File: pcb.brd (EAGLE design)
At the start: 88.9 x 70.1 mm, 104 parts, among them CN1 NC182M25, P1 39-30-02?, U1 TLV2242_D_8, U2 LT1117-S, U2.1 TCA6416A_PW_24, U3 SN74LVC1G17DBV, U4 SN74LVC1G17DBV, U6.1 DCH010505S_EDJ_4, U6.2 ISO7221A_D_8, U6.3 TS5A3357_DCU_8, U6.4 TS5A3357_DCU_8, U8.1 DCH010505S_EDJ_4, U8.2 MAX232E_D_16, U8.3 ISO7221A_D_8, U9.1 DCH010505S_EDJ_4, U9.2 ISO7220D, Y1 16MHZ

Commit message: Routing complete
All placement complete and signals routed. Awaiting copper planes,
renaming components, name placement and silkscreen.
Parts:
- removed R9.1: 47K, adafruit:M1206
- removed R9.3: 1.2K, adafruit:M1206
- added R14: 47K, rc-master-smd:R0603
- added R15: 1.2K, rc-master-smd:R0603
- moved H9.2 443.8 mm to (21.0, 68.6), turned to 180 degrees
- moved C40 440.4 mm to (13.2, 63.8)
- moved U4 437.1 mm to (13.2, 66.3), turned to 90 degrees
- moved C39 423.6 mm to (13.2, 58.7)
- moved U3 420.1 mm to (13.2, 61.2), turned to 90 degrees
- moved CN1 397.9 mm to (4.83, 45.5), turned to 90 degrees
- moved R21 369.5 mm to (71.1, 30.2), turned to 270 degrees
- moved R20 363.4 mm to (61.7, 30.2), turned to 270 degrees
- moved R19 359.4 mm to (63.5, 30.2), turned to 270 degrees
- moved R18 356.3 mm to (69.1, 30.2), turned to 270 degrees
- moved R22 345.3 mm to (24.1, 8.38), turned to 90 degrees
- moved P1 336.5 mm to (10.9, 12.2), turned to 270 degrees
- moved D4 312.4 mm to (66.3, 31.2), turned to 180 degrees
- moved D3 294.6 mm to (71.4, 18.0)
- moved D5 294.4 mm to (55.9, 8.64), turned to 90 degrees
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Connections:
- removed net 5VIO-4: D4.4, R20.1
- new net N$17: H6.1.1, R21.2
- new net N$31: H6.1.3, R18.2
- new net N$34: H6.1.5, R19.2
- new net N$35: H6.1.7, R20.2
- net 3VIO-0H: now also D3.4; no longer D3.1
- net 3VIO-2H: now also D3.1; no longer D3.4
- net 3VIO-3H: now also D2.4; no longer D2.6
- net 3VIO-4H: now also D2.3; no longer D2.1
- net 3VIO-5H: now also D2.1; no longer D2.3
- net 3VIO-6H: now also D2.6; no longer D2.4
- net 5VIO-0: now also D4.1, R21.1; no longer H6.1.7, R20.2
- net 5VIO-1: now also R18.1; no longer H6.1.5, R19.2, R21.1
- net 5VIO-2: now also D4.4, R19.1; no longer D4.1, H6.1.3, R18.1, R18.2
- net 5VIO-3: now also R20.1; no longer H6.1.1, R19.1, R21.2
- net LASER_CURRENT_3V: now also MCU.8; no longer MCU.5
- net LASER_ILK: now also R14.2; no longer R9.1.2
- net LASER_ILK_HIGH: now also R14.1; no longer R9.1.1
- net LASER_TEMPERATURE_3V: now also MCU.5; no longer MCU.8
- net N$14: now also R15.2; no longer R9.3.1
- net N$19: now also R15.1; no longer R9.3.2
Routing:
- net GND: track 123.1 -> 595.2 mm, vias 3 -> 12
- net +5V: track 86.1 -> 337.8 mm, vias 3 -> 8
- net +3V3: track 5.92 -> 249.9 mm, vias 0 -> 12
- net SGND: track 4.78 -> 45.9 mm, vias 0 -> 1
- net RS232_RX: track 37.0 -> 10.9 mm
- net TTL_GND_ISO: track 22.2 -> 43.1 mm
- net RS232_TX: track 34.2 -> 13.3 mm
- net EXT_TTL: track 10.7 -> 26.2 mm
- net 5VIO-0: track 39.0 -> 54.0 mm, vias 0 -> 4
- net N$11: track 0.00 -> 14.6 mm
- net 5VIO-2: track 31.2 -> 45.5 mm, vias 0 -> 4
- net LASER_TTL: track 63.9 -> 78.2 mm, vias 0 -> 2
- net 5VIO-3: track 26.7 -> 39.9 mm, vias 0 -> 2
- net N$14: track 0.00 -> 13.0 mm
- net N$8: track 0.00 -> 12.7 mm, vias 0 -> 1
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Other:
- board size 88.9 x 70.1 mm -> 88.9 x 81.3 mm

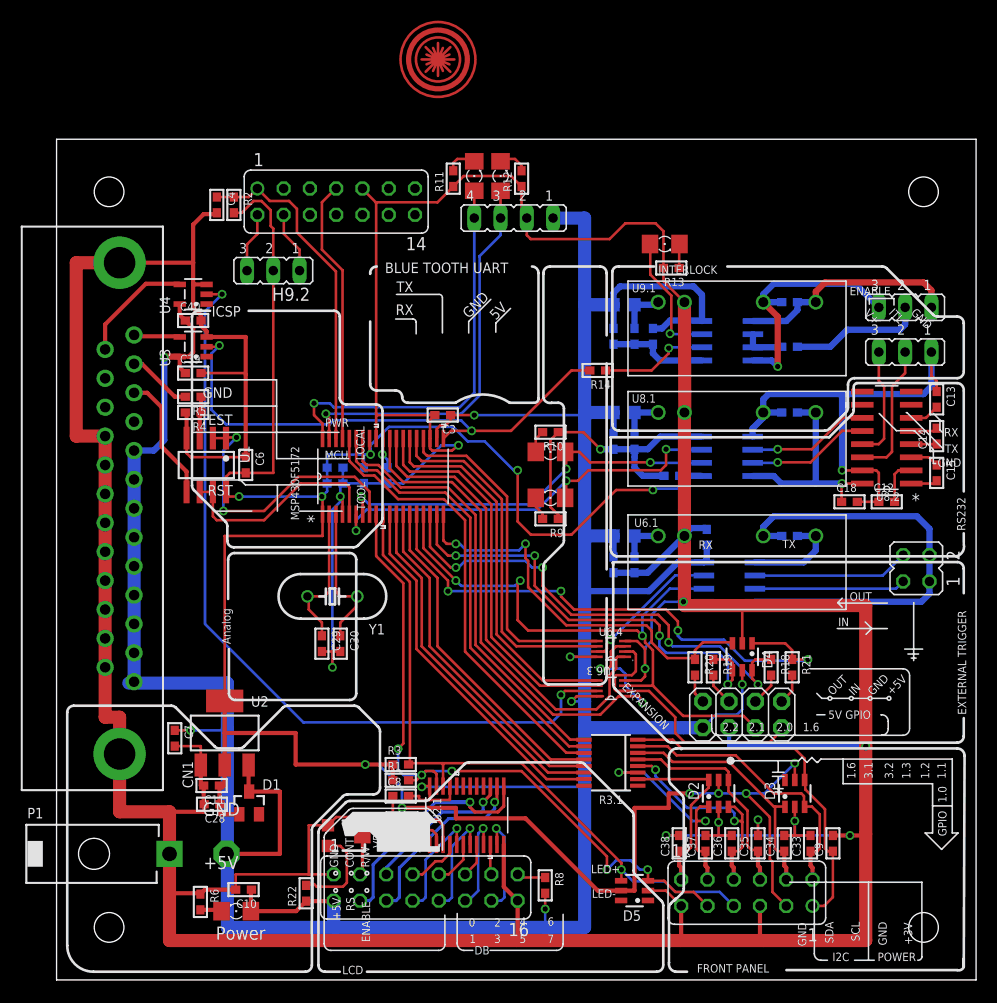
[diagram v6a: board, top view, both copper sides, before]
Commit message: Copper Pours & Component Silk Complete
Poured Copper planes and adjusted component designators for proper
silkscreen printing. Renumbered components.
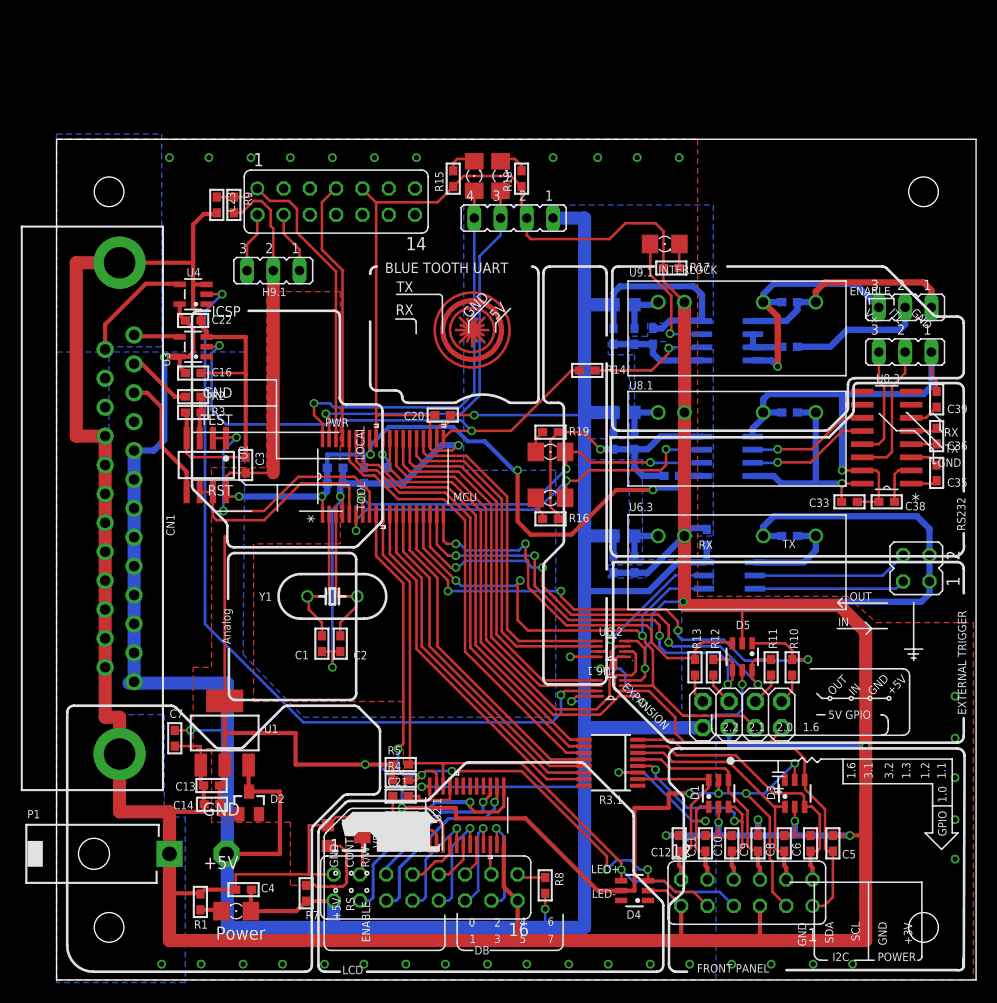
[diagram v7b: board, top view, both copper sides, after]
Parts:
- removed R21, R22: 330, rc-master-smd:R0603
- added R16, R17: 330, rc-master-smd:R0603
- C1: value .1uF -> 22pF
- C10, C5: value 10uF -> .1uF
- C14: value 1uF -> 10uF
- C15: value 1uF -> .1uF
- C17, C26: value 10uF -> 4.7uF
- C19: value 2.2uF -> .47uF
- C2: value .47uF -> 22pF
- C20, C22, C31: value 4.7uF -> .1uF
- C21: value 2.2uF -> .1uF
- C23: value .1uF -> 2.2nF
- C24: value 2.2uF -> 4.7uF
- C27: value .1uF -> 2.2uF
- C28: value 10uF -> 2.2uF
- C29: value 22pF -> 2.2uF
- C30: value 22pF -> .1uF
- C34, C37, C40: value .1uF -> 10uF
- C35, C36: value .1uF -> 1uF
- C4: value 2.2nF -> 10uF
- D1: value BAS70 -> SRV05-4; device diode:SOT23 -> diode:SOT23-6L
- D2: value SRV05-4 -> BAS70; device diode:SOT23-6L -> diode:SOT23
- H8.1: device jumper:JP2 -> jumper:JP4
- H8.2: device jumper:JP4 -> jumper:JP2
- R1, R15: value 1.2K -> 330
- R2: value 47K -> 400K
- R20: value 330 -> 1.2K
- R3: value 1.2K -> 600K
- R4: value 600K -> 1.2K
- R5: value 400K -> 1.2K
- R6: value 330 -> 10K
- R7: value 10K -> 330
- R9: value 330 -> 47K
- U1: value TLV2242_D_8 -> LT1117-S; device op-amp:SO08 -> v-reg:SOT223
- U2: value LT1117-S -> TLV2242_D_8; device v-reg:SOT223 -> op-amp:SO08
- U6.1: value DCH010505S_EDJ_4 -> TS5A3357_DCU_8; device TI:EDJ4 -> TI:DCU8
- U6.2: value ISO7221A_D_8 -> TS5A3357_DCU_8; device TI:D8 -> TI:DCU8
- U6.3: value TS5A3357_DCU_8 -> DCH010505S_EDJ_4; device TI:DCU8 -> TI:EDJ4
- U6.4: value TS5A3357_DCU_8 -> ISO7221A_D_8; device TI:DCU8 -> TI:D8
- U8.2: value MAX232E_D_16 -> ISO7221A_D_8; device TI:D16 -> TI:D8
- U8.3: value ISO7221A_D_8 -> MAX232E_D_16; device TI:D8 -> TI:D16
- moved C13 79.4 mm to (15.0, 18.8), turned to 180 degrees
- moved C14 78.6 mm to (15.0, 17.0), turned to 180 degrees
- moved C39 71.9 mm to (85.1, 56.1), turned to 270 degrees
- moved C4 66.2 mm to (18.1, 8.73), turned to 180 degrees
- moved C6 65.7 mm to (72.9, 13.2), turned to 90 degrees
- moved C15 62.8 mm to (32.5, 14.7)
- moved H9.1 61.2 mm to (21.0, 68.6)
- moved H9.2 61.2 mm to (82.0, 65.0)
- moved C40 58.3 mm to (70.9, 54.9), flipped to the bottom
- moved R11 56.4 mm to (69.1, 30.2), turned to 270 degrees
- moved R18 53.0 mm to (45.0, 77.5), turned to 90 degrees
- moved C34 52.3 mm to (70.9, 65.5), flipped to the bottom, turned to 180 degrees
- moved R12 50.8 mm to (63.5, 30.2), turned to 270 degrees
- moved C21 49.9 mm to (33.3, 17.8), flipped to the top, turned to 0 degrees
- moved C11 48.1 mm to (62.7, 13.2), turned to 90 degrees
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- renumbered JP4 to JP1
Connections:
- net +3V3: now also C13.1, C14.1, C15.2, C17.1, C18.1, C3.2, C30.2, D1.5, D2.1, D4.5, H9.1.2, R4.1, R5.1, R6.2, R9.2, U1.2, U1.4, U2.8, U8.2.1; no longer C1.1, C11.1, C16.2, C28.1, C31.1, C32.2, C6.2, D1.1, D2.5, D5.5, H9.2.2, R1.1, R2.2, R3.1, R7.2, U1.8, U2.2, U2.4, U8.3.1
- net +5V: now also C16.1, C21.2, C24.1, C26.1, C31.2, C32.2, C4.1, D2.3, D5.5, H8.1.1, R7.1, U1.3, U6.1.8; no longer C10.1, C23.2, C27.2, C3.1, C39.1, C40.1, C8.2, D1.3, D4.5, H8.2.1, R22.1, U2.3, U6.3.8
- net 3VIO-0H: now also C5.1; no longer C9.1
- net 3VIO-1H: now also C6.1; no longer C33.1
- net 3VIO-2H: now also C8.1; no longer C34.1
- net 3VIO-3H: now also C9.1, D1.4; no longer C35.1, D2.4
- net 3VIO-4H: now also C10.1, D1.3; no longer C36.1, D2.3
- net 3VIO-5H: now also C11.1, D1.1; no longer C37.1, D2.1
- net 3VIO-6H: now also C12.1, D1.6; no longer C38.1, D2.6
- net 5VIO-0: now also D5.1, R10.1; no longer D4.1, R21.1
- net 5VIO-1: now also D5.6, R11.1; no longer D4.6, R18.1
- net 5VIO-2: now also D5.4, R12.1; no longer D4.4, R19.1
- net 5VIO-3: now also D5.3, R13.1; no longer D4.3, R20.1
- net EXT_SRC-A: now also U6.2.6; no longer U6.4.6
- net EXT_SRC-B: now also U6.2.5; no longer U6.4.5
- net EXT_TTL: now also U6.1.2, U6.2.2; no longer U6.3.2, U6.4.2
- net GND: now also C12.2, C13.2, C14.2, C15.1, C16.2, C17.2, C18.2, C21.1, C23.2, C26.2, C27.2, C3.1, C30.1, C31.1, C5.2, C6.2, C8.2, D1.2, H8.1.2, R1.1, R15.1, R16.1, R17.2, R18.1, R19.1, R3.2, U1.1, U2.4, U6.1.4, U6.2.4, U6.3.2, U6.4.5, U8.2.4; no longer C16.1, C21.2, C23.1, C27.1, C3.2, C30.2, C31.2, C33.2, C34.2, C35.2, C36.2, C37.2, C38.2, C39.2, C40.2, C6.1, C8.1, D2.2, H8.2.2, R10.1, R11.1, R12.1, R13.2, R4.2, R6.1, R9.1, U1.4, U2.1, U6.1.2, U6.2.5, U6.3.4, U6.4.4, U8.3.4
- net LASER_CURRENT: now also R2.2; no longer R5.2
- net LASER_CURRENT_3V: now also U2.1, U2.2; no longer U1.1, U1.2
- net LASER_SRC-A: now also U6.1.6; no longer U6.3.6
- net LASER_SRC-B: now also U6.1.5; no longer U6.3.5
- net LASER_TEMPERATURE: now also U2.5; no longer U1.5
- net LASER_TEMPERATURE_3V: now also U2.6, U2.7; no longer U1.6, U1.7
- net LASER_TTL: now also U6.1.7; no longer U6.3.7
- net MCU_TTL1: now also U6.1.1, U6.2.3; no longer U6.3.1, U6.4.3
- net MCU_TTL2: now also U6.2.1; no longer U6.4.1
- net N$1: now also C36.1, U8.3.4; no longer C14.1, U8.2.4
- net N$11: now also U6.4.3; no longer U6.2.3
- net N$13: now also H9.1.1; no longer H9.2.1
- net N$14: now also H9.2.2, R20.2; no longer H9.1.2, R15.2
- net N$15: now also R6.1; no longer R7.1
- net N$16: now also H9.1.3; no longer H9.2.3
- net N$17: now also R10.2; no longer R21.2
- net N$18: now also R2.1, R3.1, U2.3; no longer R4.1, R5.1, U1.3
- net N$19: now also R20.1; no longer R15.1
- net N$2: now also C36.2, U8.3.5; no longer C14.2, U8.2.5
- net N$20: now also R1.2; no longer R6.2
- net N$21: now also C1.1; no longer C29.1
- net N$22: now also C2.1; no longer C30.1
- net N$23: now also LED8.2.C, R16.2; no longer LED8.1.C, R9.2
- net N$24: now also C19.1; no longer C2.1
- net N$25: now also LED8.4.C, R19.2; no longer LED8.2.C, R10.2
- net N$26: now also LED8.1.C, R15.2; no longer LED8.4.C, R11.2
- net N$27: now also C34.2, H9.2.1; no longer C26.2, H9.1.1
- net N$28: now also C34.1, H9.2.3; no longer C26.1, H9.1.3
- net N$29: now also R18.2; no longer R12.2
- net N$3: now also C35.1, U8.3.3; no longer C15.1, U8.2.3
- net N$30: now also R17.1; no longer R13.1
- net N$31: now also R11.2; no longer R18.2
- net N$32: now also C28.1, L2.1, U6.3.1; no longer C24.1, L3.1, U6.1.1
- net N$33: now also C29.1, L3.1; no longer C19.1, L1.1
- net N$34: now also R12.2; no longer R19.2
- net N$35: now also R13.2; no longer R20.2
- net N$39: now also R7.2; no longer R22.2
- net N$4: now also C35.2, U8.3.1; no longer C15.2, U8.2.1
- net N$5: now also C39.2, U8.3.6; no longer C13.2, U8.2.6
- net N$6: now also C38.2, U8.3.2; no longer C12.2, U8.2.2
- net N$9: now also C27.1, L1.1; no longer C21.1, L2.1
- net RS232_RX: now also H8.2.3, U8.3.13; no longer H8.1.3, U8.2.13
- net RS232_TX: now also H8.2.2, U8.3.14; no longer H8.1.2, U8.2.14
- net RST: now also C23.1, R9.1; no longer C4.1, R2.1
- net RX1: now also LED8.4.A, U8.2.2; no longer LED8.2.A, U8.3.2
- net RX2: now also H8.1.4, LED8.1.A; no longer H8.2.4, LED8.4.A
- net SCL: now also D4.4, R5.2; no longer D5.4, R3.2
- net SDA: now also D4.3, R4.2; no longer D5.3, R1.2
- net SERIAL_RX: now also U8.2.7, U8.3.12; no longer U8.2.12, U8.3.7
- net SERIAL_TX: now also U8.2.6, U8.3.11; no longer U8.2.11, U8.3.6
- net SGND: now also C33.2, C38.1, C39.1, C40.2, H8.2.1, U8.2.5, U8.3.15; no longer C12.1, C13.1, C17.2, C18.2, H8.1.1, U8.2.15, U8.3.5
- net TTL_GND_ISO: now also C37.1, U6.3.3, U6.4.4; no longer C5.1, U6.1.3, U6.2.4
- net TTL_IN: now also U6.1.3, U6.4.6; no longer U6.2.6, U6.3.3
- net TTL_ISO_VCC: now also C37.2, U6.3.4, U6.4.1; no longer C5.2, U6.1.4, U6.2.1
- net TTL_OUT_ISO: now also U6.4.2; no longer U6.2.2
- net TX1: now also LED8.2.A, U8.2.3; no longer LED8.1.A, U8.3.3
- net TX2: now also H8.1.3; no longer H8.2.3
- net VBUS: now also C33.1, C40.1, U8.2.8, U8.3.16; no longer C17.1, C18.1, U8.2.16, U8.3.8
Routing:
- net +3V3: track 249.9 -> 238.3 mm
- net GND: track 595.2 -> 593.7 mm, vias 12 -> 46
- net LASER_ILK_HIGH: track 10.5 -> 11.5 mm
- net LASER_ILK: track 51.0 -> 50.0 mm
- added copper zone on layer 1, net +3V3
- added copper zone on layer 16, net +5V
- added copper zone on layer 1, net GND
- added copper zone on layer 16, net GND
